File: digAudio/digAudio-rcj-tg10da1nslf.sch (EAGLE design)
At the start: 16 parts, among them IC1 DIT4096-H

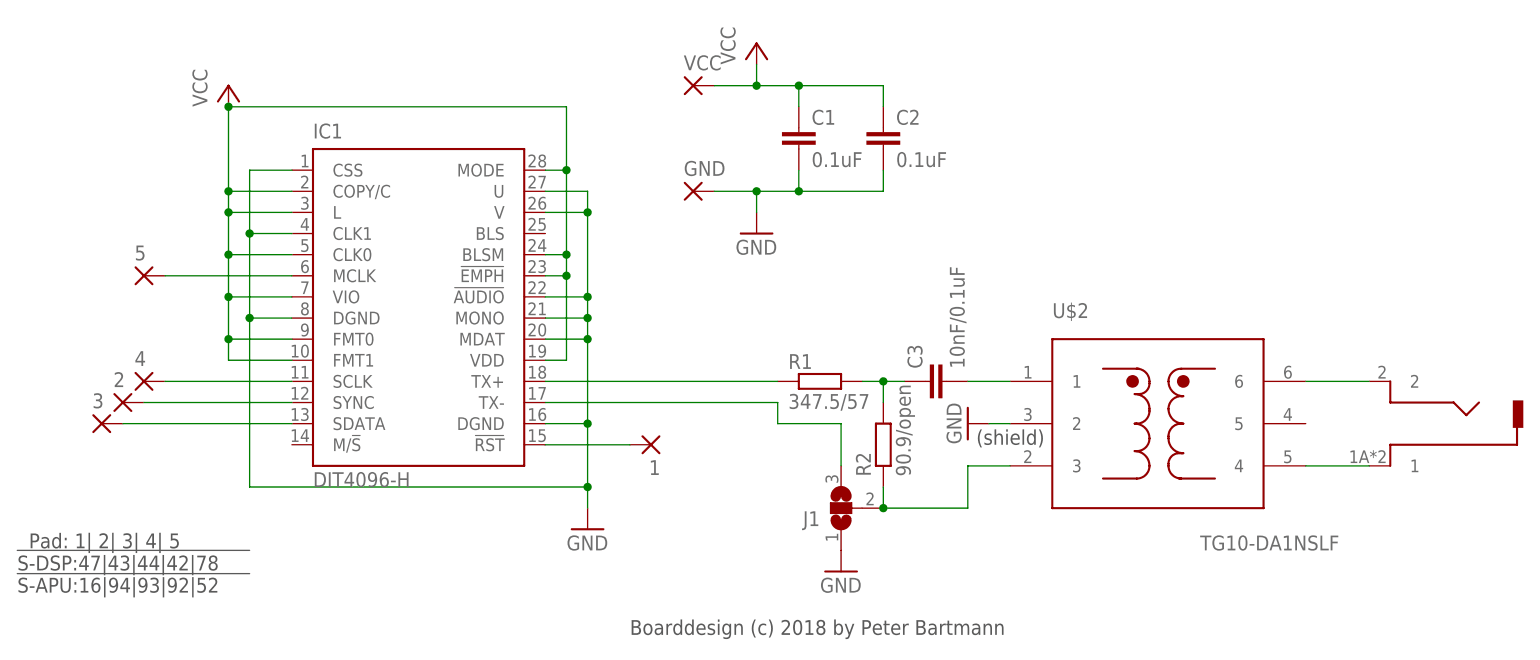
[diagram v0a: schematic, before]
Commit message: bugfix on PCBs: - pin 14 (M/nS) was floating - now it is properly connected to GND
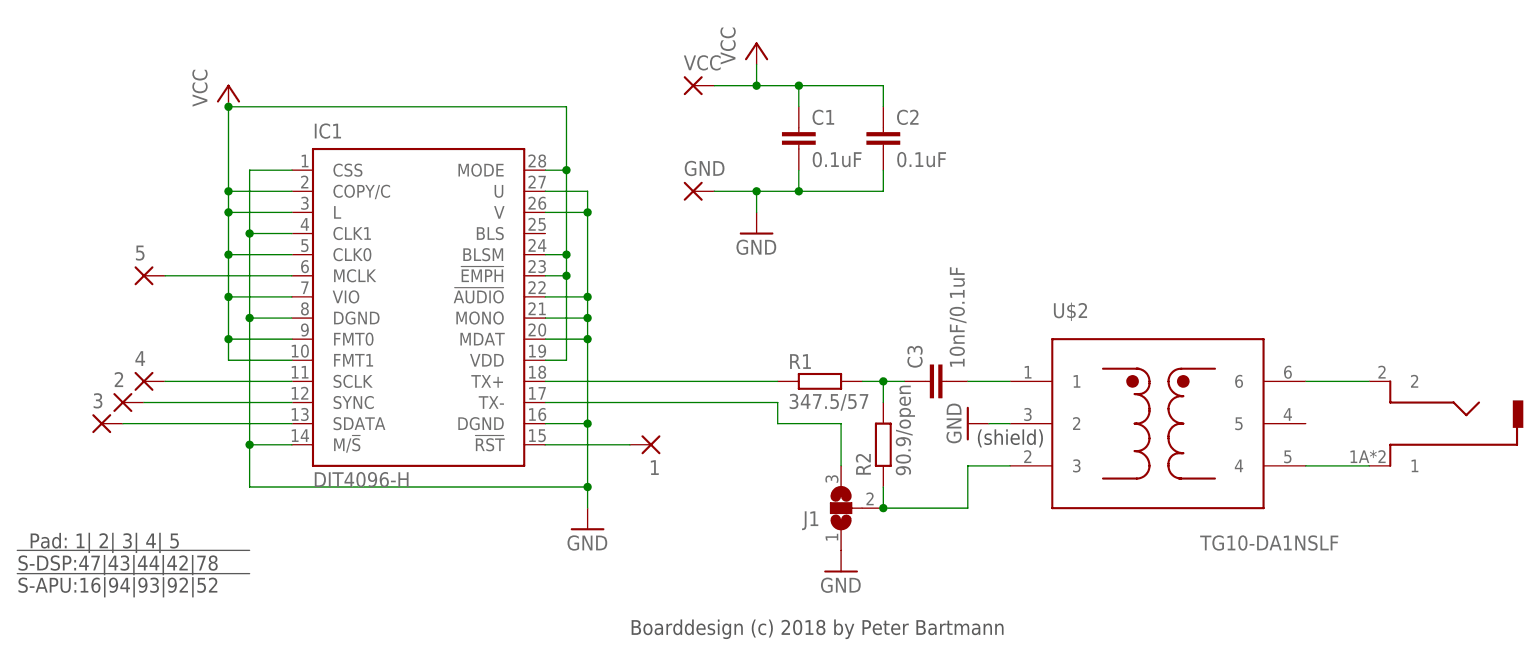
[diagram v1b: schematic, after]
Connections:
- net GND: now also IC1.M/!S
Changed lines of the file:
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@@
 <?xml version="1.0" encoding="utf-8"?>
 <!DOCTYPE eagle SYSTEM "eagle.dtd">
-<eagle version="8.5.2">
+<eagle version="9.6.2">
 <drawing>
 <settings>
@@
 </plain>
 <instances>
-<instance part="IC1" gate="G$1" x="17.78" y="50.8"/>
-<instance part="P+1" gate="VCC" x="58.42" y="81.28"/>
-<instance part="GND1" gate="1" x="38.1" y="22.86"/>
-<instance part="GND2" gate="1" x="58.42" y="58.42"/>
-<instance part="C1" gate="G$1" x="63.5" y="71.12"/>
-<instance part="C2" gate="G$1" x="73.66" y="71.12"/>
-<instance part="C3" gate="G$1" x="78.74" y="40.64" rot="R90"/>
-<instance part="P+5" gate="VCC" x="-5.08" y="76.2"/>
-<instance part="5" gate="G$1" x="-15.24" y="53.34"/>
-<instance part="4" gate="G$1" x="-15.24" y="40.64"/>
-<instance part="2" gate="G$1" x="-17.78" y="38.1"/>
-<instance part="3" gate="G$1" x="-20.32" y="35.56"/>
-<instance part="1" gate="G$1" x="45.72" y="33.02" rot="R180"/>
-<instance part="U$1" gate="G$1" x="134.62" y="38.1" rot="R180"/>
-<instance part="R1" gate="G$1" x="66.04" y="40.64"/>
-<instance part="R2" gate="G$1" x="73.66" y="33.02" rot="R90"/>
-<instance part="U$2" gate="G$1" x="106.68" y="35.56"/>
-<instance part="GND3" gate="1" x="83.82" y="35.56" rot="R270"/>
-<instance part="VCC" gate="1" x="50.8" y="76.2"/>
-<instance part="GND" gate="1" x="50.8" y="63.5"/>
-<instance part="J1" gate="G$1" x="68.58" y="25.4" rot="R180"/>
-<instance part="GND4" gate="1" x="68.58" y="17.78"/>
+<instance part="IC1" gate="G$1" x="17.78" y="50.8" smashed="yes">
+<attribute name="NAME" x="5.08" y="69.85" size="1.778" layer="95"/>
+<attribute name="VALUE" x="5.08" y="27.94" size="1.778" layer="96"/>
+</instance>
+<instance part="P+1" gate="VCC" x="58.42" y="81.28" smashed="yes">
+<attribute name="VALUE" x="55.88" y="78.74" size="1.778" layer="96" rot="R90"/>
+</instance>
+<instance part="GND1" gate="1" x="38.1" y="22.86" smashed="yes">
+<attribute name="VALUE" x="35.56" y="20.32" size="1.778" layer="96"/>
+</instance>
+<instance part="GND2" gate="1" x="58.42" y="58.42" smashed="yes">
+<attribute name="VALUE" x="55.88" y="55.88" size="1.778" layer="96"/>
+</instance>
+<instance part="C1" gate="G$1" x="63.5" y="71.12" smashed="yes">
+<attribute name="NAME" x="65.024" y="71.501" size="1.778" layer="95"/>
+<attribute name="VALUE" x="65.024" y="66.421" size="1.778" layer="96"/>
+</instance>
+<instance part="C2" gate="G$1" x="73.66" y="71.12" smashed="yes">
+<attribute name="NAME" x="75.184" y="71.501" size="1.778" layer="95"/>
+<attribute name="VALUE" x="75.184" y="66.421" size="1.778" layer="96"/>
+</instance>
+<instance part="C3" gate="G$1" x="78.74" y="40.64" smashed="yes" rot="R90">
+<attribute name="NAME" x="78.359" y="42.164" size="1.778" layer="95" rot="R90"/>
+<attribute name="VALUE" x="83.439" y="42.164" size="1.778" layer="96" rot="R90"/>
+</instance>
+<instance part="P+5" gate="VCC" x="-5.08" y="76.2" smashed="yes">
+<attribute name="VALUE" x="-7.62" y="73.66" size="1.778" layer="96" rot="R90"/>
+</instance>
+<instance part="5" gate="G$1" x="-15.24" y="53.34" smashed="yes">
+<attribute name="NAME" x="-16.383" y="55.1942" size="1.778" layer="95"/>
+<attribute name="VALUE" x="-16.383" y="50.038" size="1.778" layer="96"/>
+</instance>
+<instance part="4" gate="G$1" x="-15.24" y="40.64" smashed="yes">
+<attribute name="NAME" x="-16.383" y="42.4942" size="1.778" layer="95"/>
+<attribute name="VALUE" x="-16.383" y="37.338" size="1.778" layer="96"/>
+</instance>
+<instance part="2" gate="G$1" x="-17.78" y="38.1" smashed="yes">
+<attribute name="NAME" x="-18.923" y="39.9542" size="1.778" layer="95"/>
+<attribute name="VALUE" x="-18.923" y="34.798" size="1.778" layer="96"/>
+</instance>
+<instance part="3" gate="G$1" x="-20.32" y="35.56" smashed="yes">
+<attribute name="NAME" x="-21.463" y="37.4142" size="1.778" layer="95"/>
+<attribute name="VALUE" x="-21.463" y="32.258" size="1.778" layer="96"/>
+</instance>
+<instance part="1" gate="G$1" x="45.72" y="33.02" smashed="yes" rot="R180">
+<attribute name="NAME" x="46.863" y="31.1658" size="1.778" layer="95" rot="R180"/>
+<attribute name="VALUE" x="46.863" y="36.322" size="1.778" layer="96" rot="R180"/>
+</instance>
+<instance part="U$1" gate="G$1" x="134.62" y="38.1" smashed="yes" rot="R180"/>
+<instance part="R1" gate="G$1" x="66.04" y="40.64" smashed="yes">
+<attribute name="NAME" x="62.23" y="42.1386" size="1.778" layer="95"/>
+<attribute name="VALUE" x="62.23" y="37.338" size="1.778" layer="96"/>
+</instance>
+<instance part="R2" gate="G$1" x="73.66" y="33.02" smashed="yes" rot="R90">
+<attribute name="NAME" x="72.1614" y="29.21" size="1.778" layer="95" rot="R90"/>
+<attribute name="VALUE" x="76.962" y="29.21" size="1.778" layer="96" rot="R90"/>
+</instance>
+<instance part="U$2" gate="G$1" x="106.68" y="35.56" smashed="yes">
+<attribute name="NAME" x="93.98" y="48.26" size="1.778" layer="95"/>
+<attribute name="VALUE" x="111.76" y="20.32" size="1.778" layer="96"/>
+</instance>
+<instance part="GND3" gate="1" x="83.82" y="35.56" smashed="yes" rot="R270">
+<attribute name="VALUE" x="81.28" y="38.1" size="1.778" layer="96" rot="R270"/>
+</instance>
+<instance part="VCC" gate="1" x="50.8" y="76.2" smashed="yes">
+<attribute name="NAME" x="49.657" y="78.0542" size="1.778" layer="95"/>
+<attribute name="VALUE" x="49.657" y="72.898" size="1.778" layer="96"/>
+</instance>
+<instance part="GND" gate="1" x="50.8" y="63.5" smashed="yes">
+<attribute name="NAME" x="49.657" y="65.3542" size="1.778" layer="95"/>
+<attribute name="VALUE" x="49.657" y="60.198" size="1.778" layer="96"/>
+</instance>
+<instance part="J1" gate="G$1" x="68.58" y="25.4" smashed="yes" rot="R180">
+<attribute name="NAME" x="66.04" y="25.019" size="1.778" layer="95" rot="R180"/>
+<attribute name="VALUE" x="66.04" y="27.305" size="1.778" layer="96" rot="R180"/>
+</instance>
+<instance part="GND4" gate="1" x="68.58" y="17.78" smashed="yes">
+<attribute name="VALUE" x="66.04" y="15.24" size="1.778" layer="96"/>
+</instance>
 </instances>
 <busses>
@@
 <wire x1="-2.54" y1="66.04" x2="-2.54" y2="58.42" width="0.1524" layer="91"/>
 <wire x1="-2.54" y1="58.42" x2="-2.54" y2="48.26" width="0.1524" layer="91"/>
-<wire x1="-2.54" y1="48.26" x2="-2.54" y2="27.94" width="0.1524" layer="91"/>
+<wire x1="-2.54" y1="48.26" x2="-2.54" y2="33.02" width="0.1524" layer="91"/>
 <pinref part="IC1" gate="G$1" pin="CSS"/>
+<wire x1="-2.54" y1="33.02" x2="-2.54" y2="27.94" width="0.1524" layer="91"/>
 <wire x1="-2.54" y1="66.04" x2="2.54" y2="66.04" width="0.1524" layer="91"/>
 <pinref part="IC1" gate="G$1" pin="CLK1"/>
@@
 <wire x1="38.1" y1="27.94" x2="-2.54" y2="27.94" width="0.1524" layer="91"/>
 <junction x="38.1" y="27.94"/>
+<pinref part="IC1" gate="G$1" pin="M/!S"/>
+<wire x1="2.54" y1="33.02" x2="-2.54" y2="33.02" width="0.1524" layer="91"/>
+<junction x="-2.54" y="33.02"/>
 </segment>
 <segment>
